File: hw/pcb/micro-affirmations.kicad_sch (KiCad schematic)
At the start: 21 parts, among them J1 USBC, J2 DEBUG, SW1 RST, U1 STM32C031C6Tx

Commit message: fix: swapped capacitor voltage pins
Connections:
- net CAP_VOLT: now also U1.11 (PA0); no longer U1.46 (PB7)
- net at TP7.1: now also U1.46 (PB7); no longer U1.11 (PA0)
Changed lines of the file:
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@@
 	(title_block
 		(title "μAffirmations")
-		(rev "RevC")
+		(rev "RevD")
 		(company "Isaac Pawley")
 	)
@@
 	(wire
 		(pts
+			(xy 124.46 92.71) (xy 105.41 92.71)
+		)
+		(stroke
+			(width 0)
+			(type default)
+		)
+	)
+	(wire
+		(pts
 			(xy 46.99 102.87) (xy 80.01 102.87)
 		)
@@
 		)
 	)
-	(wire
-		(pts
-			(xy 105.41 153.67) (xy 113.03 153.67)
-		)
-		(stroke
-			(width 0)
-			(type default)
-		)
-	)
 	(label "MATRIX_A1"
 		(at 124.46 161.29 180)
@@
 	(global_label "CAP_VOLT"
 		(shape input)
-		(at 113.03 153.67 0)
+		(at 124.46 92.71 0)
 		(fields_autoplaced yes)
 		(effects
@@
 		)
 		(property "Intersheetrefs" "${INTERSHEET_REFS}"
-			(at 125.0262 153.67 0)
+			(at 136.4562 92.71 0)
 			(hide yes)
 			(show_name no)
@@
 	)
 	(symbol
+		(lib_id "Connector:TestPoint")
+		(at 105.41 153.67 270)
+		(unit 1)
+		(body_style 1)
+		(exclude_from_sim no)
+		(in_bom yes)
+		(on_board yes)
+		(in_pos_files yes)
+		(dnp no)
+		(property "Reference" "TP7"
+			(at 110.998 153.67 0)
+			(show_name no)
+			(do_not_autoplace no)
+			(effects
+				(font
+					(size 1.27 1.27)
+				)
+			)
+		)
+		(property "Value" "TestPoint"
+			(at 109.9819 151.13 0)
+			(hide yes)
+			(show_name no)
+			(do_not_autoplace no)
+			(effects
+				(font
+					(size 1.27 1.27)
+				)
+				(justify right)
+			)
+		)
+		(property "Footprint" "TestPoint:TestPoint_Pad_D1.0mm"
+			(at 105.41 158.75 0)
+			(hide yes)
+			(show_name no)
+			(do_not_autoplace no)
+			(effects
+				(font
+					(size 1.27 1.27)
+				)
+			)
+		)
+		(property "Datasheet" ""
+			(at 105.41 158.75 0)
+			(hide yes)
+			(show_name no)
+			(do_not_autoplace no)
+			(effects
+				(font
+					(size 1.27 1.27)
+				)
+			)
+		)
+		(property "Description" "test point"
+			(at 105.41 153.67 0)
+			(hide yes)
+			(show_name no)
+			(do_not_autoplace no)
+			(effects
+				(font
+					(size 1.27 1.27)
+				)
+			)
+		)
+		(pin "1"
+		)
+		(instances
+			(project "micro-affirmations"
+				(path "/5bc9bd8c-4e85-4538-85a6-329775c75541"
+					(reference "TP7")
+					(unit 1)
+				)
+			)
+		)
+	)
+	(symbol
 		(lib_id "power:GND")
 		(at 125.73 83.82 0)
@@
 					(unit 1)
 				)
-			)
-		)
-	)
-	(symbol
-		(lib_id "Connector:TestPoint")
-		(at 105.41 92.71 270)
-		(unit 1)
-		(body_style 1)
-		(exclude_from_sim no)
-		(in_bom yes)
-		(on_board yes)
-		(in_pos_files yes)
-		(dnp no)
-		(property "Reference" "TP7"
-			(at 110.998 92.71 0)
-			(show_name no)
-			(do_not_autoplace no)
-			(effects
-				(font
-					(size 1.27 1.27)
-				)
-			)
-		)
-		(property "Value" "TestPoint"
-			(at 109.9819 90.17 0)
-			(hide yes)
-			(show_name no)
-			(do_not_autoplace no)
-			(effects
-				(font
-					(size 1.27 1.27)
-				)
-				(justify right)
-			)
-		)
-		(property "Footprint" "TestPoint:TestPoint_Pad_D1.0mm"
-			(at 105.41 97.79 0)
-			(hide yes)
-			(show_name no)
-			(do_not_autoplace no)
-			(effects
-				(font
-					(size 1.27 1.27)
-				)
-			)
-		)
-		(property "Datasheet" ""
-			(at 105.41 97.79 0)
-			(hide yes)
-			(show_name no)
-			(do_not_autoplace no)
-			(effects
-				(font
-					(size 1.27 1.27)
-				)
-			)
-		)
-		(property "Description" "test point"
-			(at 105.41 92.71 0)
-			(hide yes)
-			(show_name no)
-			(do_not_autoplace no)
-			(effects
-				(font
-					(size 1.27 1.27)
-				)
-			)
-		)
-		(pin "1"
-		)
-		(instances
-			(project "micro-affirmations"
-				(path "/5bc9bd8c-4e85-4538-85a6-329775c75541"
-					(reference "TP7")
-					(unit 1)
-				)

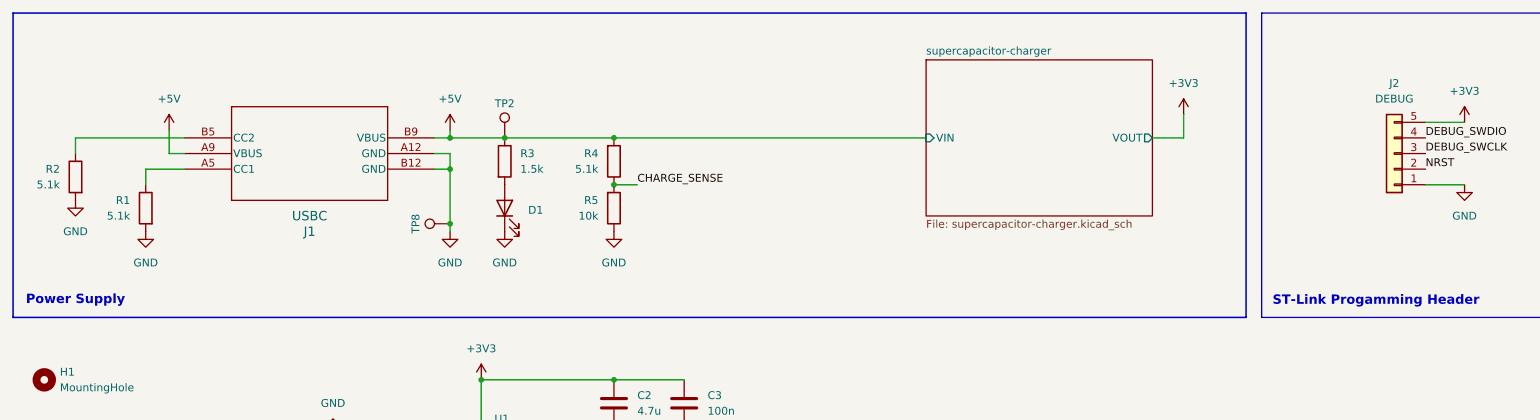
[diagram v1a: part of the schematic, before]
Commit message: fix: updated schematics to pcb revision d
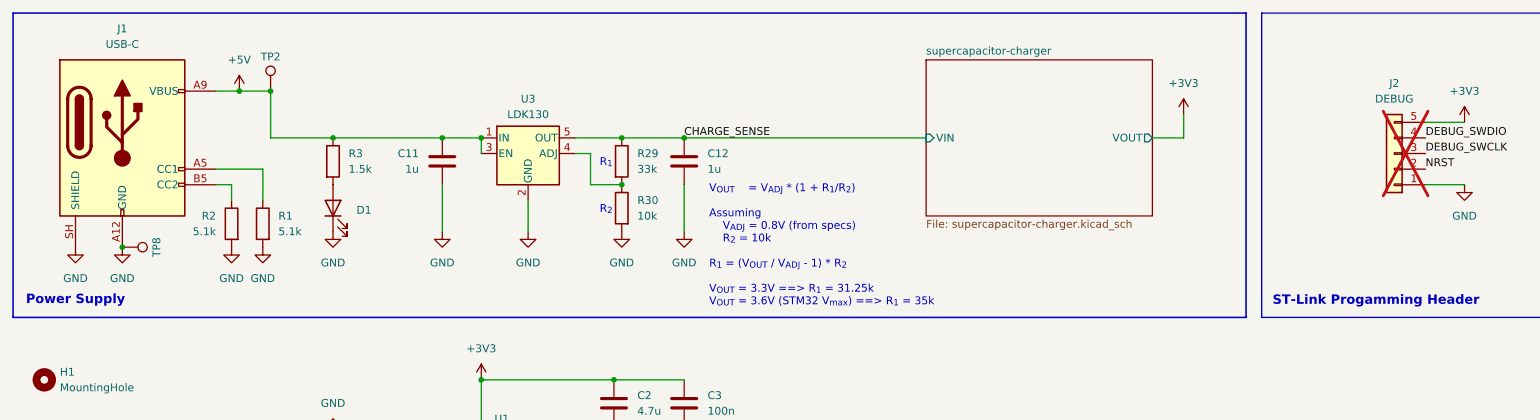
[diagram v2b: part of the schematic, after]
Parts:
- removed J1: USBC, micro-affirmations_footprints:2171750001_MOL, symbol micro-affirmations_symbols:USB-C_2171750001
- removed R4: 5.1k, Resistor_SMD:R_0603_1608Metric, symbol Device:R
- removed R5: 10k, Resistor_SMD:R_0603_1608Metric, symbol Device:R
- added C11, C12: 1u, Capacitor_SMD:C_0603_1608Metric, symbol Device:C
- added J1: USB-C, micro-affirmations_footprints:2171750001_MOL, symbol Connector:USB_C_Receptacle_PowerOnly_6P
- added R29: 33k, Resistor_SMD:R_0603_1608Metric, symbol Device:R
- added R30: 10k, Resistor_SMD:R_0603_1608Metric, symbol Device:R
- added U3: LDK130, Package_TO_SOT_SMD:SOT-23-5, symbol Regulator_Linear:LDK130-ADJ_SOT23_SOT353
- H1: PN (none) -> -
- J2: PN (none) -> -; now not fitted
- TP2, TP4, TP5, TP6, TP7, TP8: PN (none) -> -; now left out of the parts list
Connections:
- net +5V: now also C11.1, J1.A9 (VBUS), J1.B9 (VBUS), U3.1 (IN), U3.3 (EN)
- net CHARGE_SENSE: now also C12.1, R29.1, U3.5 (OUT)
- net GND: now also C11.2, C12.2, J1.A12 (GND), J1.B12 (GND), J1.SH (SHIELD), R30.2, U3.2 (GND)
- net at R2.1: now also J1.B5 (CC2)
- net at R1.1: now also J1.A5 (CC1)
- new net: R29.2, R30.1, U3.4 (ADJ)
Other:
- note added: "R_{1}"
- note added: "R_{2}"
- note added: "V_{OUT} = V_{ADJ} * (1 + R_{1}/R_{2}) Assuming V_{ADJ} = 0.8V (from specs) R_{2} = 10k R_{1} = (V_{OUT} / V_{ADJ} - 1) * R_{2} V_{OUT} = 3.3V ==> R_{1} = 31.25k V_{OUT} = 3.6V (STM32 V_{max}) ==> R_{1} = 35k"
- moved on the sheet: R1, R2

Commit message: chore: added stars to potentially different components
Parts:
- R29: value 33k -> 33k*
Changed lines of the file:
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@@
 			)
 		)
-		(property "Value" "33k"
+		(property "Value" "33k*"
 			(at 118.11 41.9099 0)
 			(show_name no)
